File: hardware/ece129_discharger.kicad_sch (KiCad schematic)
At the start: 11 parts, among them J1 Conn_01x03, J10 Conn_01x02, J11 Conn_01x02, J2 Conn_01x02, J3 Conn_01x02, J4 Conn_01x02, J5 Conn_01x02, J6 Conn_01x02, J7 Conn_01x02, J8 Conn_01x02, J9 Conn_01x02

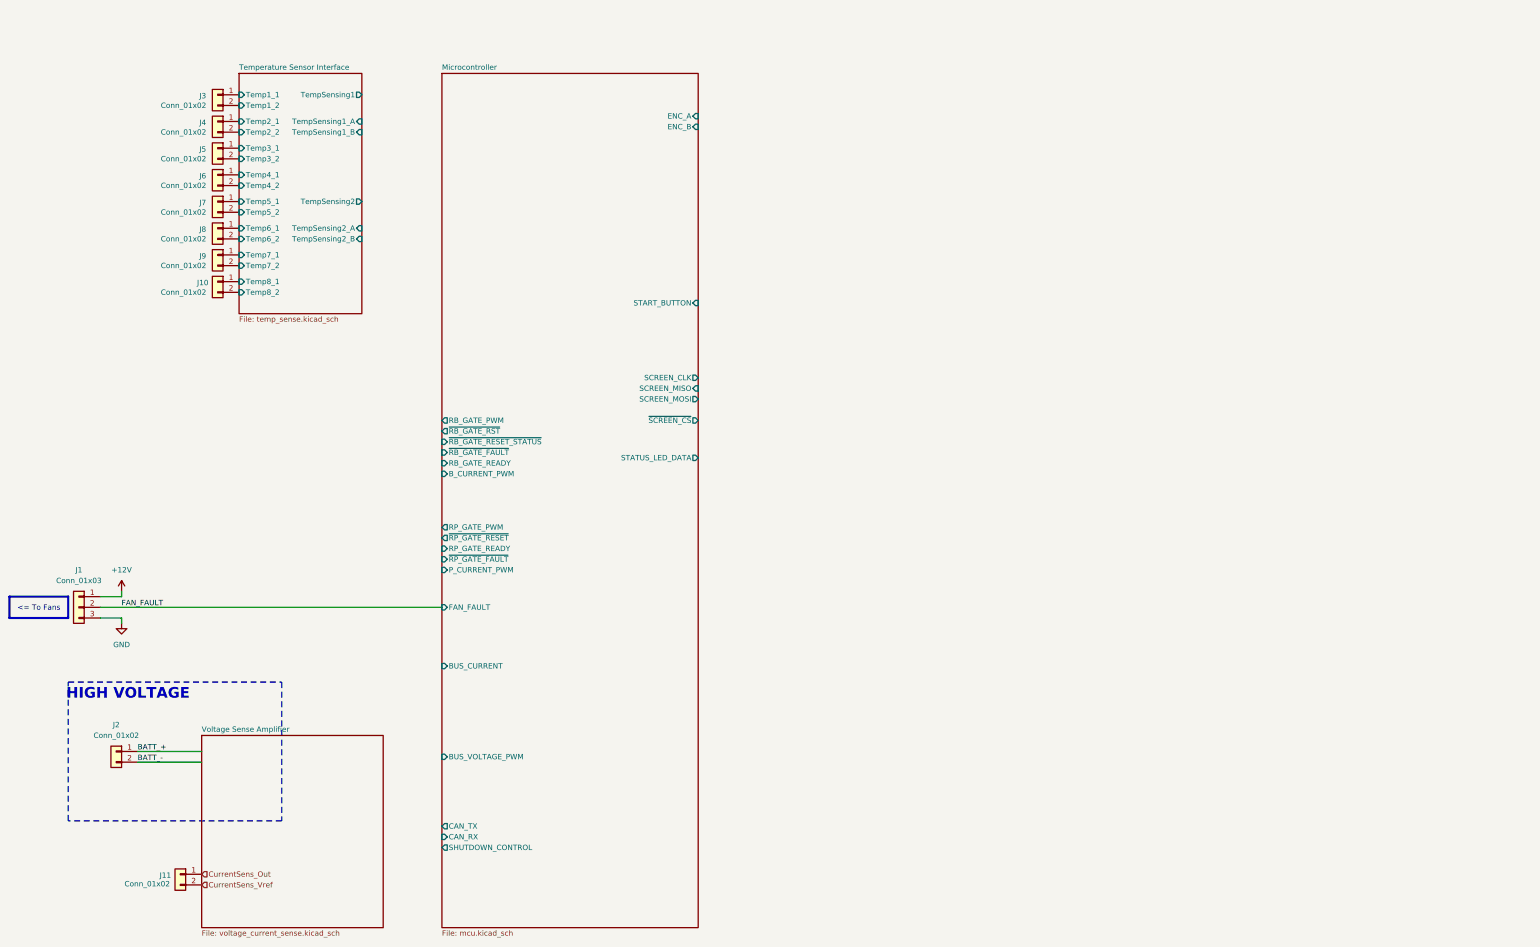
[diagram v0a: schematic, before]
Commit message: completed main board schematic
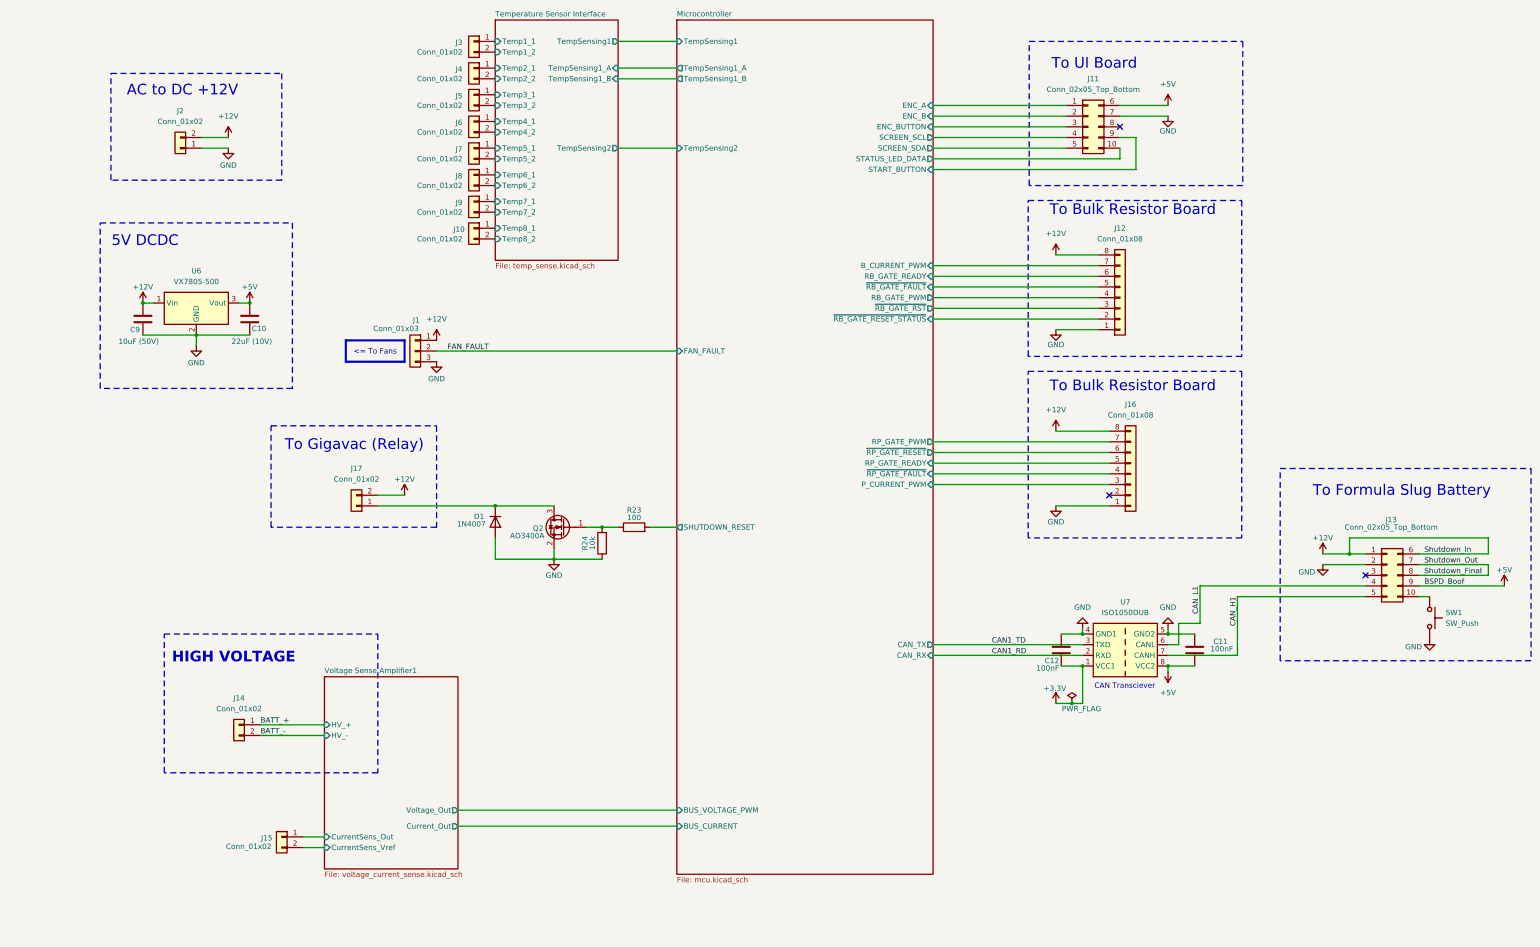
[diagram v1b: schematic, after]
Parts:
- removed J11: Conn_01x02, symbol Connector_Generic:Conn_01x02
- added C10: 22uF (10V), symbol Device:C
- added C11, C12: 100nF, Capacitor_SMD:C_0805_2012Metric_Pad1.18x1.45mm_HandSolder, symbol Device:C
- added C9: 10uF (50V), symbol Device:C
- added D1: 1N4007, Diode_THT:D_DO-41_SOD81_P10.16mm_Horizontal, symbol Diode:1N4007
- added J11, J13: Conn_02x05_Top_Bottom, symbol Connector_Generic:Conn_02x05_Top_Bottom
- added J12, J16: Conn_01x08, symbol Connector_Generic:Conn_01x08
- added J14, J15, J17: Conn_01x02, symbol Connector_Generic:Conn_01x02
- added Q2: AO3400A, Package_TO_SOT_SMD:SOT-23, symbol Transistor_FET:AO3400A
- added R23: 100, symbol Device:R
- added R24: 10k, symbol Device:R
- added SW1: SW_Push, symbol Switch:SW_Push
- added U6: VX7805-500, Converter_DCDC:Converter_DCDC_TRACO_TSR0.5-24xx_TSR0.5-24xxx_THT, symbol discharger:VX7805-500
- added U7: ISO1050DUB, Package_SO:SOP-8_6.62x9.15mm_P2.54mm, symbol Interface_CAN_LIN:ISO1050DUB
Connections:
- net +12V: now also J2.2 (Pin_2), C9.1, J12.8 (Pin_8), J13.1 (Pin_1), J13.6 (Pin_6), J16.8 (Pin_8), J17.2 (Pin_2), U6.1 (Vin)
- net BATT_+: now also J14.1 (Pin_1); no longer J2.1 (Pin_1)
- net BATT_-: now also J14.2 (Pin_2); no longer J2.2 (Pin_2)
- net GND: now also J2.1 (Pin_1), C10.2, C11.1, C12.1, C9.2, D1.2 (A), J11.7 (Pin_7), J12.1 (Pin_1), J13.2 (Pin_2), J16.1 (Pin_1), Q2.2 (S), R24.1, SW1.2, U6.2 (GND), U7.4 (GND1), U7.5 (GND2)
- net Microcontroller/B_CURRENT_PWM: now also J12.7 (Pin_7)
- net Microcontroller/ENC_A: now also J11.1 (Pin_1)
- net Microcontroller/ENC_B: now also J11.2 (Pin_2)
- net Microcontroller/P_CURRENT_PWM: now also J16.3 (Pin_3)
- net Microcontroller/RB_GATE_PWM: now also J12.4 (Pin_4)
- net Microcontroller/RB_GATE_READY: now also J12.6 (Pin_6)
- net Microcontroller/RP_GATE_PWM: now also J16.7 (Pin_7)
- net Microcontroller/RP_GATE_READY: now also J16.5 (Pin_5)
- net Microcontroller/START_BUTTON: now also J11.9 (Pin_9)
- net Microcontroller/STATUS_LED_DATA: now also J11.10 (Pin_10)
- net Microcontroller/~{RB_GATE_FAULT}: now also J12.5 (Pin_5)
- net Microcontroller/~{RB_GATE_RESET_STATUS}: now also J12.2 (Pin_2)
- net Microcontroller/~{RB_GATE_RST}: now also J12.3 (Pin_3)
- net Microcontroller/~{RP_GATE_FAULT}: now also J16.4 (Pin_4)
- net Microcontroller/~{RP_GATE_RESET}: now also J16.6 (Pin_6)
- new net: D1.1 (K), J17.1 (Pin_1), Q2.3 (D)
- new net: Q2.1 (G), R23.1, R24.2
- new net: J13.10 (Pin_10), SW1.1
- new net +3.3V: C12.2, U7.1 (VCC1)
- new net +5V: C10.1, C11.2, J11.6 (Pin_6), J13.9 (Pin_9), U6.3 (Vout), U7.8 (VCC2)
- new net CAN1_RD: U7.2 (RXD)
- new net CAN1_TD: U7.3 (TXD)
- new net CAN_H1: J13.5 (Pin_5), U7.7 (CANH)
- new net CAN_L1: J13.4 (Pin_4), U7.6 (CANL)
- new net Microcontroller/ENC_BUTTON: J11.3 (Pin_3)
- new net Microcontroller/SCREEN_SCL: J11.4 (Pin_4)
- new net Microcontroller/SCREEN_SDA: J11.5 (Pin_5)
- new net Microcontroller/SHUTDOWN_RESET: R23.2
- new net Shutdown_Final: J13.7 (Pin_7), J13.8 (Pin_8)
- new net Voltage Sense Amplifier1/CurrentSens_Out: J15.1 (Pin_1)
- new net Voltage Sense Amplifier1/CurrentSens_Vref: J15.2 (Pin_2)
- no-connect marks 0 -> 3
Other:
- removed sheet Voltage Sense Amplifier
- added sheet Voltage Sense Amplifier1 (voltage_current_sense.kicad_sch)
- sheet Microcontroller ports: added ENC_BUTTON, SCREEN_SCL, SCREEN_SDA, SHUTDOWN_RESET, TempSensing1, TempSensing1_A, TempSensing1_B, TempSensing2; removed SCREEN_CLK, SCREEN_MISO, SCREEN_MOSI, SHUTDOWN_CONTROL, ~{SCREEN_CS}
- sheet Temperature Sensor Interface ports: added none; removed TempSensing2_A, TempSensing2_B
- note added: "5V DCDC"
- note added: "AC to DC +12V"
- note added: "CAN Transciever"
- note added: "To Bulk Resistor Board"
- note added: "To Formula Slug Battery"
- note added: "To Gigavac (Relay)"
- note added: "To UI Board"
- moved on the sheet: J1, J10, J3, J4, J5, J6, J7, J8, J9

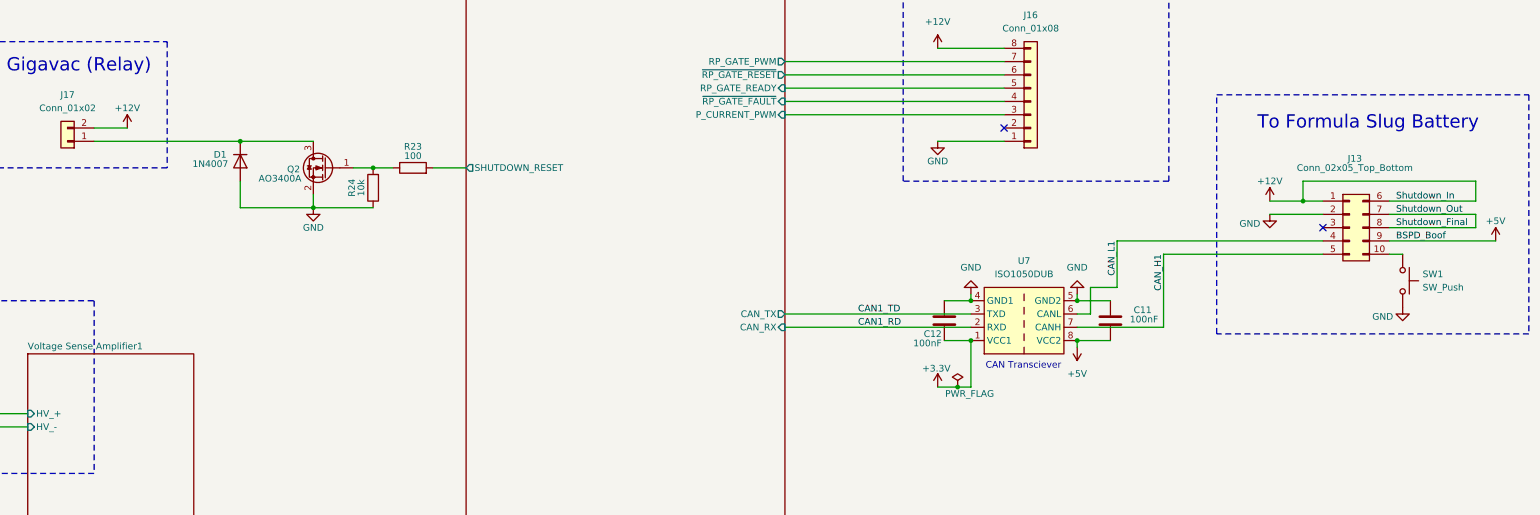
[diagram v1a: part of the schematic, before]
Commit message: changes to battery connector
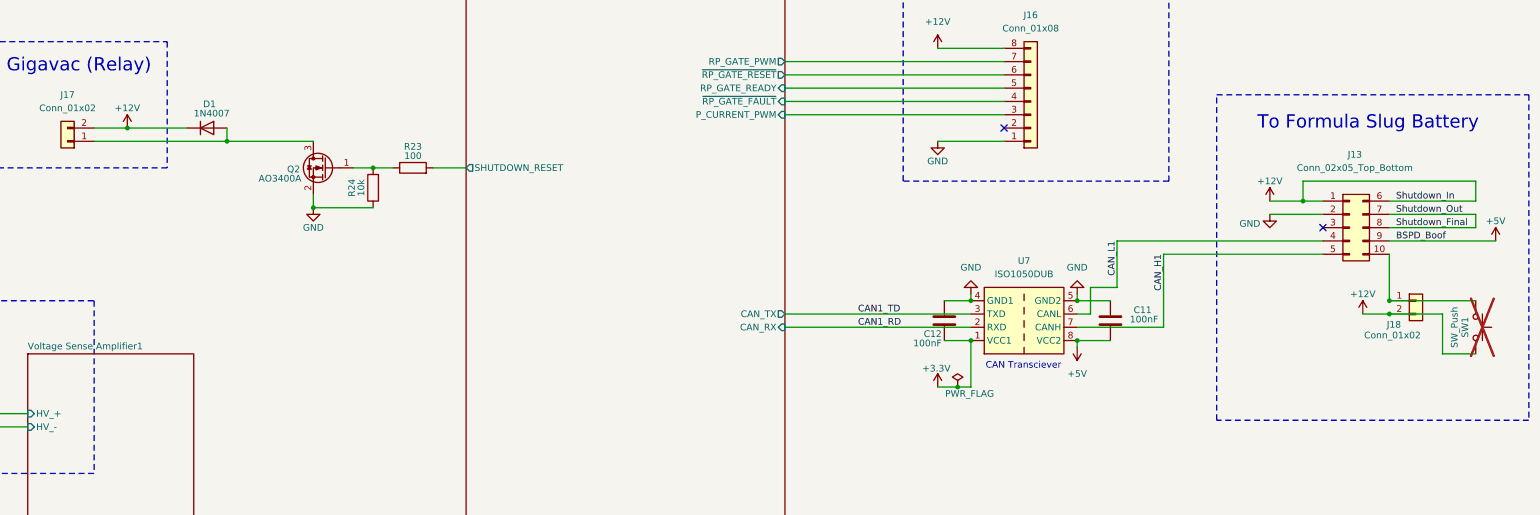
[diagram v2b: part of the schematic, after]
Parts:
- added J18: Conn_01x02, symbol Connector_Generic:Conn_01x02
- SW1: now not fitted
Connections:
- net +12V: now also D1.1 (K), SW1.2, J18.2 (Pin_2)
- net GND: no longer D1.2 (A), SW1.2
- net at J17.1 (Pin_1), Q2.3 (D): now also D1.2 (A); no longer D1.1 (K)
- net at J13.10 (Pin_10), SW1.1: now also J18.1 (Pin_1)
